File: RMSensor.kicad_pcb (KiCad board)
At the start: 2 copper layers, 32 x 32 mm, 26 parts, among them J1 Conn_01x02, J2 Conn_01x02, J3 Conn_01x04, U1 OPA209AID, U2 OPA2350UA, U3 MC78L05_TO92, U4 TLE2425xD

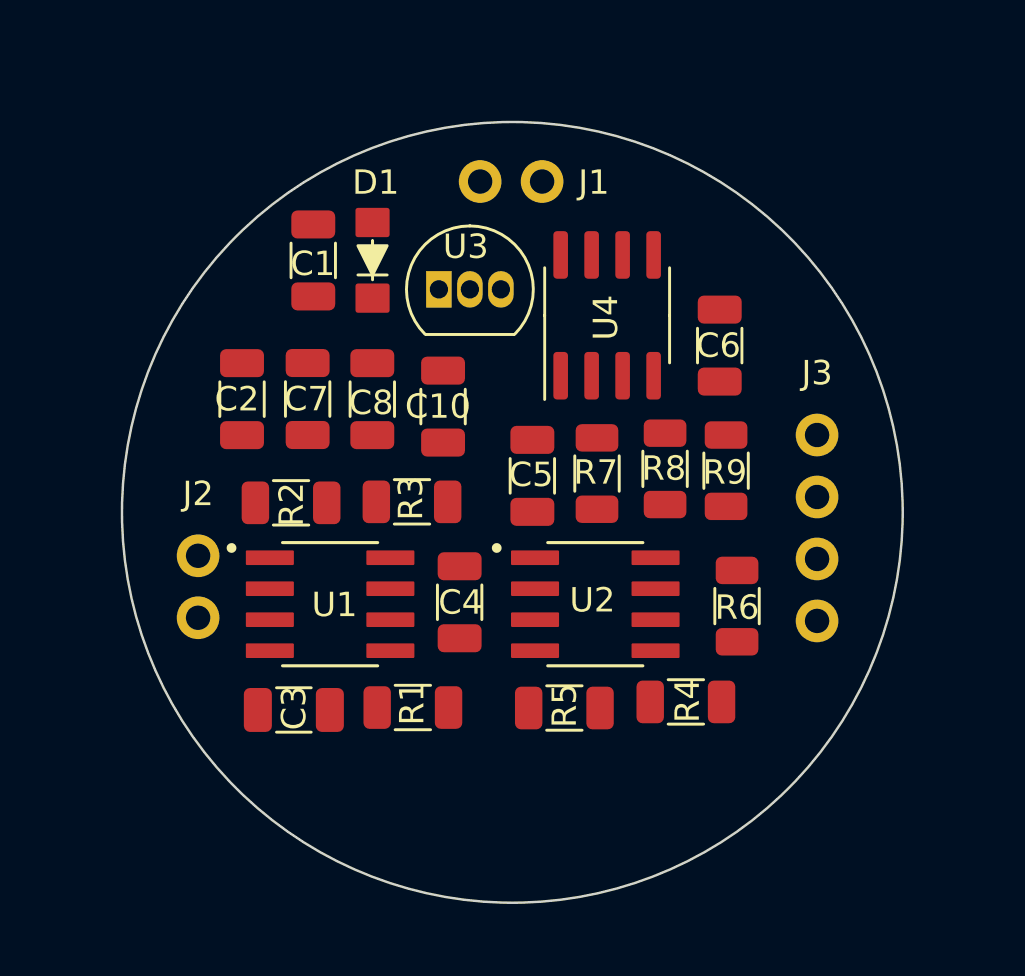
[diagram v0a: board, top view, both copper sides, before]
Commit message: changed res and cap footprint to 805 and changed regulator
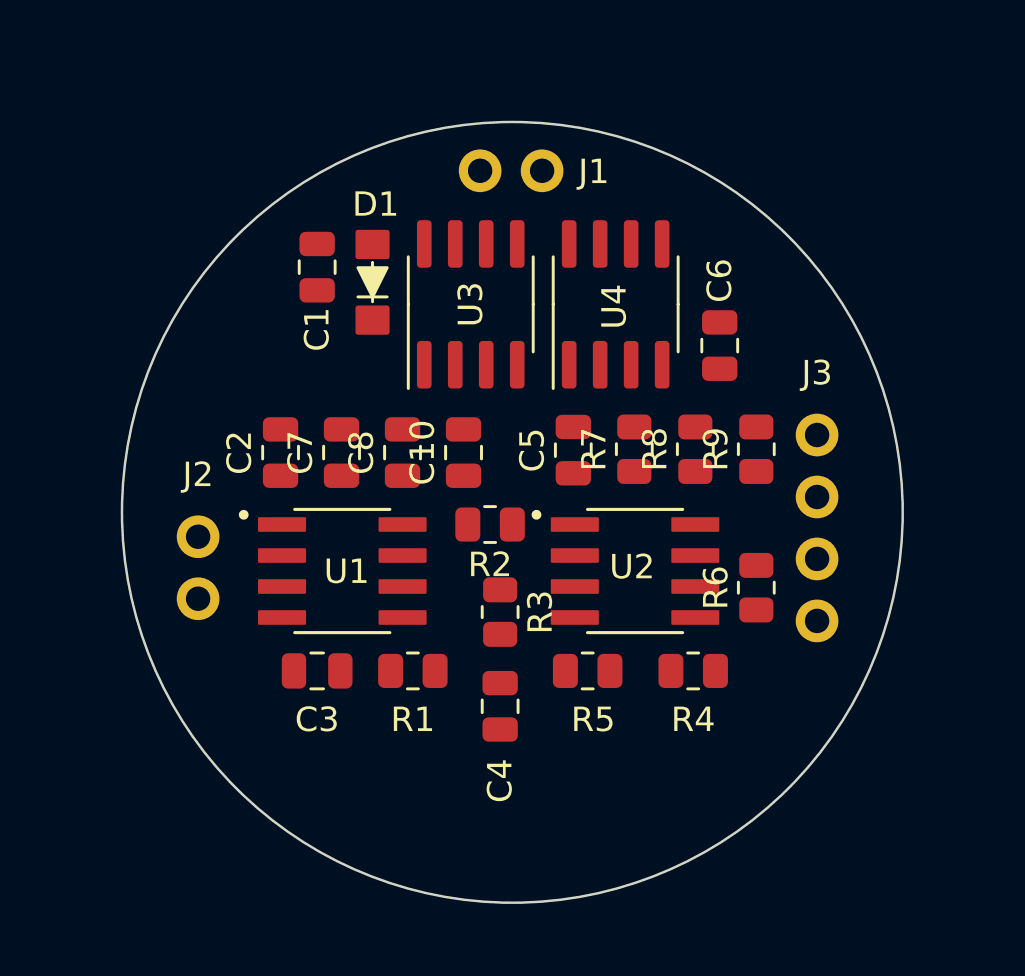
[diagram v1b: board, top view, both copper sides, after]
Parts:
- C1, C10, C2, C3, C4, C5, C6, C7, C8: footprint Capacitor_SMD:C_1206_3216Metric -> Capacitor_SMD:C_0805_2012Metric
- R1, R2, R3, R4, R5, R6, R7, R8, R9: footprint Resistor_SMD:R_1206_3216Metric -> Resistor_SMD:R_0805_2012Metric
- U3: value MC78L05_TO92 -> MC78L05_SO8; footprint Package_TO_SOT_THT:TO-92_Inline -> Package_SO:SOIC-8_3.9x4.9mm_P1.27mm
- moved R2 8.21 mm to (149.1, 101.5)
- moved R3 5.78 mm to (149.5, 105.1), turned to -90 degrees
- moved C4 4.58 mm to (149.5, 109.0)
- moved C2 2.70 mm to (140.5, 98.5)
- moved C7 2.60 mm to (143.0, 98.5)
- moved C8 2.52 mm to (145.5, 98.5)
- moved U2 2.12 mm to (155.0, 103.4)
- moved C10 2.06 mm to (148.0, 98.5)
- moved C5 1.98 mm to (152.5, 98.5)
- moved C3 1.86 mm to (142.0, 107.5)
- moved R7 1.83 mm to (155.0, 98.4)
- moved R5 1.80 mm to (153.1, 107.5)
- moved R9 1.52 mm to (160.0, 98.4)
- moved R1 1.50 mm to (145.9, 107.5)
- moved R8 1.48 mm to (157.5, 98.4)
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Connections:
- U3 pad 3: Net-(C1-Pad1) -> GND

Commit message: pcb with traces
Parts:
- C2, C8: value 100n -> 1u
- moved R4 12.5 mm to (152.4, 96.0)
- moved C10 12.1 mm to (159.8, 101.3)
- moved R7 12.0 mm to (159.8, 109.4)
- moved C8 11.9 mm to (157.4, 99.5)
- moved R1 11.5 mm to (139.1, 98.2)
- moved C5 11.2 mm to (154.5, 109.5), turned to -90 degrees
- moved R9 10.6 mm to (149.4, 99.3), turned to -90 degrees
- moved R2 10.2 mm to (142.6, 109.4), turned to 90 degrees
- moved R8 9.35 mm to (149.4, 103.1)
- moved R5 9.20 mm to (153.2, 98.3)
- moved C3 7.21 mm to (138.4, 101.2), turned to 90 degrees
- moved C1 7.00 mm to (149.0, 90.8)
- moved C2 5.15 mm to (145.7, 98.4), turned to 0 degrees
- moved R3 4.90 mm to (147.2, 109.4)
- moved U3 4.79 mm to (143.8, 94.2), turned to 0 degrees
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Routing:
- net +5V: track 0.00 -> 63.4 mm, vias 0 -> 3
- net GND: track 0.00 -> 25.2 mm, vias 0 -> 5
- net Net-(C6-Pad2): track 0.00 -> 16.2 mm
- net Net-(C5-Pad1): track 0.00 -> 14.8 mm
- net Net-(R1-Pad2): track 0.00 -> 14.1 mm
- net Net-(R4-Pad2): track 0.00 -> 10.0 mm
- net Net-(C4-Pad1): track 0.00 -> 9.52 mm
- net Net-(R8-Pad1): track 0.00 -> 9.05 mm
- net Net-(C3-Pad1): track 0.00 -> 8.98 mm
- net Net-(C4-Pad2): track 0.00 -> 7.90 mm
- net Net-(D1-Pad2): track 0.00 -> 6.97 mm
- net Net-(C6-Pad1): track 0.00 -> 6.27 mm
- net Net-(R6-Pad1): track 0.00 -> 5.56 mm
- net Net-(C1-Pad1): track 0.00 -> 5.12 mm
- added copper zone on F.Cu, net +2V5
- added copper zone on B.Cu, net GND
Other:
- board size 32 x 32 mm -> 34 x 34 mm

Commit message: 31mm board
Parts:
- moved C3 2.31 mm to (140.6, 100.4), turned to 0 degrees
- moved J2 1.81 mm to (137.0, 100.1)
- moved R1 1.40 mm to (140.5, 98.2)
- moved R7 1.14 mm to (159.0, 108.6)
- moved C4 0.85 mm to (144.1, 109.2)
- moved R2 0.85 mm to (141.8, 109.1)
- moved R3 0.85 mm to (146.4, 109.1)
- moved C2 0.82 mm to (144.8, 98.2)
- moved C6 0.82 mm to (156.9, 95.7)
- moved C8 0.82 mm to (156.6, 99.3)
- moved D1 0.82 mm to (144.2, 90.0)
- moved R5 0.82 mm to (152.4, 98.1)
- moved R6 0.82 mm to (159.0, 104.9)
- moved R8 0.82 mm to (148.6, 102.9)
- moved C1 0.82 mm to (148.2, 90.7)
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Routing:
- net +2V5: track 0.39 -> 5.84 mm
- net GND: track 25.2 -> 29.3 mm, vias 5 -> 6
- net +5V: track 63.4 -> 65.3 mm
- net Net-(C5-Pad1): track 14.8 -> 13.6 mm
- net Net-(R1-Pad2): track 14.1 -> 13.1 mm
- net Net-(D1-Pad2): track 6.97 -> 7.81 mm
- net Net-(R6-Pad1): track 5.56 -> 4.95 mm
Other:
- board size 34 x 34 mm -> 31 x 31 mm
- board text added: "+2V5"
- board text added: "+5V"
- board text added: "GND"
- board text added: "IN"
- board text added: "OUT"
- board text added: "Vs"
